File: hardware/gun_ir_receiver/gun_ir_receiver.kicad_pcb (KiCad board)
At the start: 2 copper layers, 19 x 17.8 mm, 3 parts

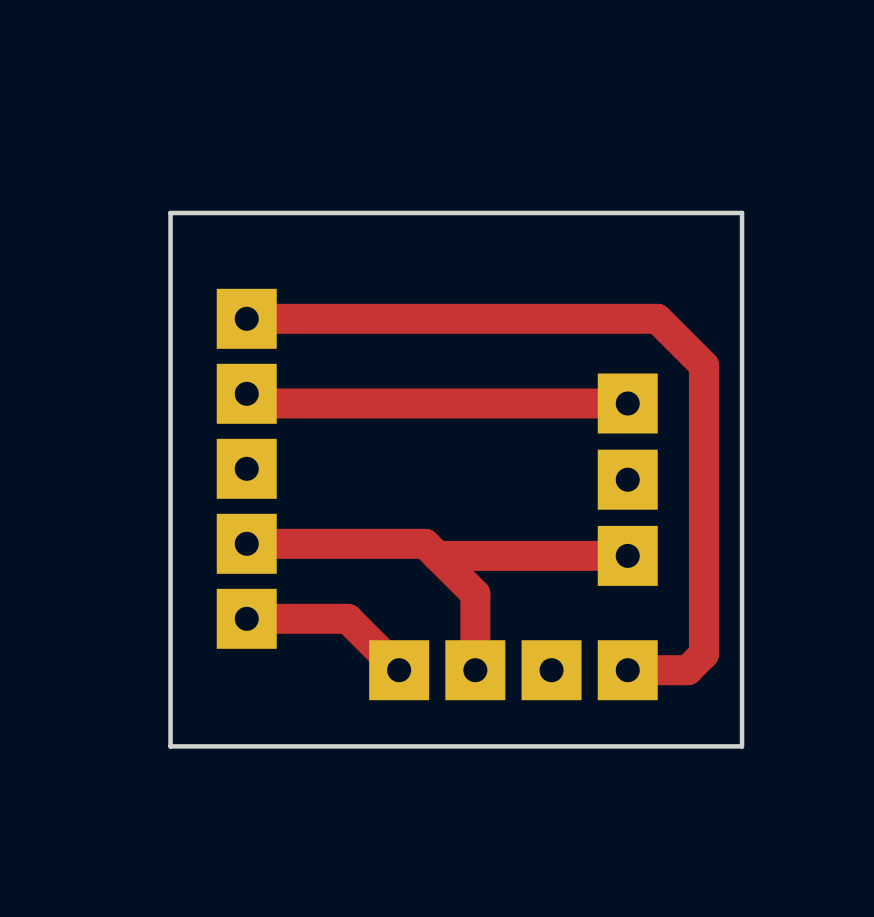
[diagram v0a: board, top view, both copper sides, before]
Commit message: Added led
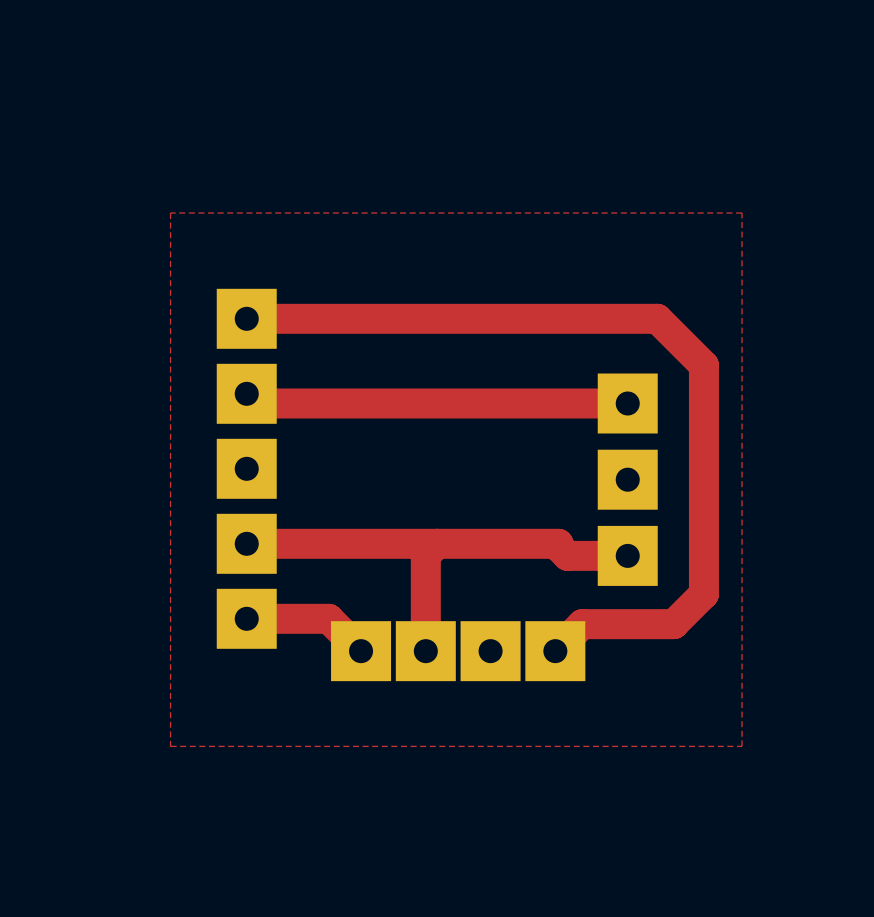
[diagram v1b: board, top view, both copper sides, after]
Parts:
- LEDPL9823: footprint Connector_PinSocket_2.54mm:PinSocket_1x04_P2.54mm_Vertical -> LED_THT:LED_D5.0mm-4_RGB_Wide_Pins
- moved LEDPL9823 1.42 mm to (118.1, 111.1), turned to 0 degrees
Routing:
- net /LedIn: track 5.79 -> 4.26 mm
- net /LedOut: track 28.3 -> 29.2 mm
- net +5V: track 17.2 -> 16.7 mm
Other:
- board outline removed
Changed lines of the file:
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@@
   (general
     (thickness 1.6)
-    (drawings 1)
-    (tracks 14)
+    (drawings 0)
+    (tracks 17)
     (zones 0)
     (modules 3)
@@
     (42 Eco1.User user)
     (43 Eco2.User user)
-    (44 Edge.Cuts user hide)
+    (44 Edge.Cuts user)
     (45 Margin user)
     (46 B.CrtYd user)
@@
     (add_net GND)
   )
-  (module Connector_PinSocket_2.54mm:PinSocket_1x04_P2.54mm_Vertical (layer B.Cu)
-    (at 119.38 111.76 270)
-    (descr "Through hole straight socket strip, 1x04, 2.54mm pitch, single row (from Kicad 4.0.7), script generated")
-    (tags "Through hole socket strip THT 1x04 2.54mm single row")
-    (fp_text reference LEDPL9823 (at 0 2.77 270) (layer B.SilkS)
-      (effects (font (size 1 1) (thickness 0.15)) (justify mirror))
-    )
-    (fp_text value Conn_01x04_Female (at 0 -10.39 270) (layer B.Fab)
-      (effects (font (size 1 1) (thickness 0.15)) (justify mirror))
-    )
-    (fp_line (start -1.27 1.27) (end 0.635 1.27) (layer B.Fab) (width 0.1))
-    (fp_line (start 0.635 1.27) (end 1.27 0.635) (layer B.Fab) (width 0.1))
-    (fp_line (start 1.27 0.635) (end 1.27 -8.89) (layer B.Fab) (width 0.1))
-    (fp_line (start 1.27 -8.89) (end -1.27 -8.89) (layer B.Fab) (width 0.1))
-    (fp_line (start -1.27 -8.89) (end -1.27 1.27) (layer B.Fab) (width 0.1))
-    (fp_line (start -1.33 -1.27) (end 1.33 -1.27) (layer B.SilkS) (width 0.12))
-    (fp_line (start -1.33 -1.27) (end -1.33 -8.95) (layer B.SilkS) (width 0.12))
-    (fp_line (start -1.33 -8.95) (end 1.33 -8.95) (layer B.SilkS) (width 0.12))
-    (fp_line (start 1.33 -1.27) (end 1.33 -8.95) (layer B.SilkS) (width 0.12))
-    (fp_line (start 1.33 1.33) (end 1.33 0) (layer B.SilkS) (width 0.12))
-    (fp_line (start 0 1.33) (end 1.33 1.33) (layer B.SilkS) (width 0.12))
-    (fp_line (start -1.8 1.8) (end 1.75 1.8) (layer B.CrtYd) (width 0.05))
-    (fp_line (start 1.75 1.8) (end 1.75 -9.4) (layer B.CrtYd) (width 0.05))
-    (fp_line (start 1.75 -9.4) (end -1.8 -9.4) (layer B.CrtYd) (width 0.05))
-    (fp_line (start -1.8 -9.4) (end -1.8 1.8) (layer B.CrtYd) (width 0.05))
-    (fp_text user %R (at 0 -3.81 180) (layer B.Fab)
-      (effects (font (size 1 1) (thickness 0.15)) (justify mirror))
-    )
-    (pad 1 thru_hole rect (at 0 0 270) (size 2 2) (drill 0.8) (layers *.Cu *.Mask)
+  (module LED_THT:LED_D5.0mm-4_RGB_Wide_Pins (layer B.Cu)
+    (at 118.11 111.125)
+    (descr "LED, diameter 5.0mm, 2 pins, diameter 5.0mm, 3 pins, diameter 5.0mm, 4 pins, http://www.kingbright.com/attachments/file/psearch/000/00/00/L-154A4SUREQBFZGEW(Ver.9A).pdf")
+    (tags "LED diameter 5.0mm 2 pins diameter 5.0mm 3 pins diameter 5.0mm 4 pins RGB RGBLED")
+    (fp_text reference LEDPL9823 (at 3.2385 3.96) (layer B.SilkS)
+      (effects (font (size 1 1) (thickness 0.15)) (justify mirror))
+    )
+    (fp_text value Conn_01x04_Female (at 3.2385 -3.96) (layer B.Fab)
+      (effects (font (size 1 1) (thickness 0.15)) (justify mirror))
+    )
+    (fp_arc (start 3.2385 0) (end 0.7385 1.469694) (angle -299.1) (layer B.Fab) (width 0.1))
+    (fp_arc (start 3.2385 0) (end 0.6785 1.54483) (angle -127.7) (layer B.SilkS) (width 0.12))
+    (fp_arc (start 3.2385 0) (end 0.6785 -1.54483) (angle 127.7) (layer B.SilkS) (width 0.12))
+    (fp_arc (start 3.2385 0) (end 0.983816 1.08) (angle -128.8) (layer B.SilkS) (width 0.12))
+    (fp_arc (start 3.2385 0) (end 0.983816 -1.08) (angle 128.8) (layer B.SilkS) (width 0.12))
+    (fp_circle (center 3.2385 0) (end 5.7385 0) (layer B.Fab) (width 0.1))
+    (fp_line (start 0.7385 1.469694) (end 0.7385 -1.469694) (layer B.Fab) (width 0.1))
+    (fp_line (start 0.6785 1.545) (end 0.6785 1.08) (layer B.SilkS) (width 0.12))
+    (fp_line (start 0.6785 -1.08) (end 0.6785 -1.545) (layer B.SilkS) (width 0.12))
+    (fp_line (start -1.08 3.25) (end -1.08 -3.25) (layer B.CrtYd) (width 0.05))
+    (fp_line (start -1.08 -3.25) (end 7.56 -3.25) (layer B.CrtYd) (width 0.05))
+    (fp_line (start 7.56 -3.25) (end 7.56 3.25) (layer B.CrtYd) (width 0.05))
+    (fp_line (start 7.56 3.25) (end -1.08 3.25) (layer B.CrtYd) (width 0.05))
+    (fp_text user %R (at 3.2385 3.96) (layer B.Fab)
+      (effects (font (size 1 1) (thickness 0.15)) (justify mirror))
+    )
+    (pad 1 thru_hole rect (at 0 0) (size 2 2) (drill 0.8) (layers *.Cu *.Mask)
       (net 5 /LedIn))
-    (pad 2 thru_hole rect (at 0 -2.54 270) (size 2 2) (drill 0.8) (layers *.Cu *.Mask)
+    (pad 2 thru_hole rect (at 2.159 0) (size 2 2) (drill 0.8) (layers *.Cu *.Mask)
       (net 2 +5V))
-    (pad 3 thru_hole rect (at 0 -5.08 270) (size 2 2) (drill 0.8) (layers *.Cu *.Mask)
+    (pad 3 thru_hole rect (at 4.318 0) (size 2 2) (drill 0.8) (layers *.Cu *.Mask)
       (net 4 GND))
-    (pad 4 thru_hole rect (at 0 -7.62 270) (size 2 2) (drill 0.8) (layers *.Cu *.Mask)
+    (pad 4 thru_hole rect (at 6.477 0) (size 2 2) (drill 0.8) (layers *.Cu *.Mask)
       (net 3 /LedOut))
-    (model ${KISYS3DMOD}/Connector_PinSocket_2.54mm.3dshapes/PinSocket_1x04_P2.54mm_Vertical.wrl
+    (model ${KISYS3DMOD}/LED_THT.3dshapes/LED_D5.0mm-4_RGB_Wide_Pins.wrl
       (at (xyz 0 0 0))
       (scale (xyz 1 1 1))
@@
     )
   )
-  (gr_poly (pts (xy 111.76 96.52) (xy 130.81 96.52) (xy 130.81 114.3) (xy 111.76 114.3)) (layer Edge.Cuts) (width 0.15))
   (segment (start 114.622704 102.87) (end 114.3 102.547296) (width 1) (layer F.Cu) (net 1))
   (segment (start 127 102.87) (end 114.622704 102.87) (width 1) (layer F.Cu) (net 1))
-  (segment (start 114.3 107.547296) (end 120.247296 107.547296) (width 1) (layer F.Cu) (net 2))
-  (segment (start 121.92 109.22) (end 121.92 111.76) (width 1) (layer F.Cu) (net 2))
-  (segment (start 120.65 107.95) (end 127 107.95) (width 1) (layer F.Cu) (net 2))
-  (segment (start 120.65 107.95) (end 121.92 109.22) (width 1) (layer F.Cu) (net 2))
-  (segment (start 120.247296 107.547296) (end 120.65 107.95) (width 1) (layer F.Cu) (net 2))
+  (segment (start 125 107.95) (end 127 107.95) (width 1) (layer F.Cu) (net 2))
+  (segment (start 124.692296 107.642296) (end 125 107.95) (width 1) (layer F.Cu) (net 2))
+  (segment (start 124.692296 107.547296) (end 124.692296 107.642296) (width 1) (layer F.Cu) (net 2))
+  (segment (start 120.269 107.928296) (end 120.65 107.547296) (width 1) (layer F.Cu) (net 2))
+  (segment (start 120.269 111.125) (end 120.269 107.928296) (width 1) (layer F.Cu) (net 2))
+  (segment (start 114.3 107.547296) (end 120.65 107.547296) (width 1) (layer F.Cu) (net 2))
+  (segment (start 120.65 107.547296) (end 124.692296 107.547296) (width 1) (layer F.Cu) (net 2))
+  (segment (start 125.486999 110.225001) (end 128.534999 110.225001) (width 1) (layer F.Cu) (net 3))
+  (segment (start 124.587 111.125) (end 125.486999 110.225001) (width 1) (layer F.Cu) (net 3))
+  (segment (start 128.534999 110.225001) (end 129.54 109.22) (width 1) (layer F.Cu) (net 3))
+  (segment (start 129.54 109.22) (end 129.54 101.6) (width 1) (layer F.Cu) (net 3))
   (segment (start 127.987296 100.047296) (end 114.3 100.047296) (width 1) (layer F.Cu) (net 3))
   (segment (start 129.54 101.6) (end 127.987296 100.047296) (width 1) (layer F.Cu) (net 3))
-  (segment (start 129.54 111.22) (end 129.54 101.6) (width 1) (layer F.Cu) (net 3))
-  (segment (start 127 111.76) (end 129 111.76) (width 1) (layer F.Cu) (net 3))
-  (segment (start 129 111.76) (end 129.54 111.22) (width 1) (layer F.Cu) (net 3))
-  (segment (start 117.667296 110.047296) (end 119.38 111.76) (width 1) (layer F.Cu) (net 5))
-  (segment (start 114.3 110.047296) (end 117.667296 110.047296) (width 1) (layer F.Cu) (net 5))
+  (segment (start 117.032296 110.047296) (end 118.11 111.125) (width 1) (layer F.Cu) (net 5))
+  (segment (start 114.3 110.047296) (end 117.032296 110.047296) (width 1) (layer F.Cu) (net 5))
   (zone (net 4) (net_name GND) (layer F.Cu) (hatch edge 0.508)
     (connect_pads yes (clearance 0.544))
@@
     (polygon
       (pts
-        (xy 111.76 96.52) (xy 130.81 96.506127) (xy 130.81 114.286127) (xy 111.76 114.3)
+        (xy 111.76 114.3) (xy 130.81 114.3) (xy 130.81 96.52) (xy 111.76 96.52)
       )
     )

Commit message: Added led
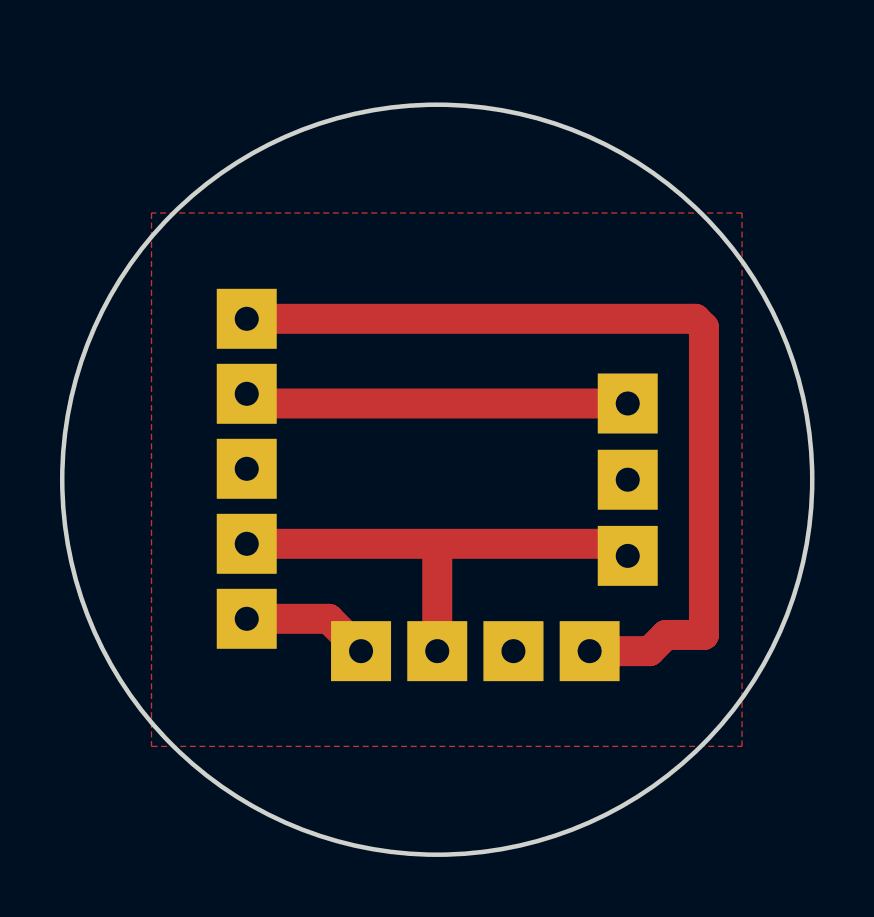
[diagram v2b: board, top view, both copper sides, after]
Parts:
- LEDPL9823: footprint LED_THT:LED_D5.0mm-4_RGB_Wide_Pins -> Connector_PinSocket_2.54mm:PinSocket_1x04_P2.54mm_Vertical
- turned LEDPL9823 to 270 degrees
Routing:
- net +5V: track 16.7 -> 16.0 mm
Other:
- board outline added: 25 x 25 mm
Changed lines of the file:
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@@
   (general
     (thickness 1.6)
-    (drawings 0)
-    (tracks 17)
+    (drawings 2)
+    (tracks 13)
     (zones 0)
     (modules 3)
@@
     (pad_to_mask_clearance 0.051)
     (solder_mask_min_width 0.25)
-    (aux_axis_origin 111.76 114.3)
+    (aux_axis_origin 111.125 114.3)
     (visible_elements FFFFFF7F)
     (pcbplotparams
@@
     (add_net GND)
   )
-  (module LED_THT:LED_D5.0mm-4_RGB_Wide_Pins (layer B.Cu)
-    (at 118.11 111.125)
-    (descr "LED, diameter 5.0mm, 2 pins, diameter 5.0mm, 3 pins, diameter 5.0mm, 4 pins, http://www.kingbright.com/attachments/file/psearch/000/00/00/L-154A4SUREQBFZGEW(Ver.9A).pdf")
-    (tags "LED diameter 5.0mm 2 pins diameter 5.0mm 3 pins diameter 5.0mm 4 pins RGB RGBLED")
-    (fp_text reference LEDPL9823 (at 3.2385 3.96) (layer B.SilkS)
-      (effects (font (size 1 1) (thickness 0.15)) (justify mirror))
-    )
-    (fp_text value Conn_01x04_Female (at 3.2385 -3.96) (layer B.Fab)
-      (effects (font (size 1 1) (thickness 0.15)) (justify mirror))
-    )
-    (fp_arc (start 3.2385 0) (end 0.7385 1.469694) (angle -299.1) (layer B.Fab) (width 0.1))
-    (fp_arc (start 3.2385 0) (end 0.6785 1.54483) (angle -127.7) (layer B.SilkS) (width 0.12))
-    (fp_arc (start 3.2385 0) (end 0.6785 -1.54483) (angle 127.7) (layer B.SilkS) (width 0.12))
-    (fp_arc (start 3.2385 0) (end 0.983816 1.08) (angle -128.8) (layer B.SilkS) (width 0.12))
-    (fp_arc (start 3.2385 0) (end 0.983816 -1.08) (angle 128.8) (layer B.SilkS) (width 0.12))
-    (fp_circle (center 3.2385 0) (end 5.7385 0) (layer B.Fab) (width 0.1))
-    (fp_line (start 0.7385 1.469694) (end 0.7385 -1.469694) (layer B.Fab) (width 0.1))
-    (fp_line (start 0.6785 1.545) (end 0.6785 1.08) (layer B.SilkS) (width 0.12))
-    (fp_line (start 0.6785 -1.08) (end 0.6785 -1.545) (layer B.SilkS) (width 0.12))
-    (fp_line (start -1.08 3.25) (end -1.08 -3.25) (layer B.CrtYd) (width 0.05))
-    (fp_line (start -1.08 -3.25) (end 7.56 -3.25) (layer B.CrtYd) (width 0.05))
-    (fp_line (start 7.56 -3.25) (end 7.56 3.25) (layer B.CrtYd) (width 0.05))
-    (fp_line (start 7.56 3.25) (end -1.08 3.25) (layer B.CrtYd) (width 0.05))
-    (fp_text user %R (at 3.2385 3.96) (layer B.Fab)
-      (effects (font (size 1 1) (thickness 0.15)) (justify mirror))
-    )
-    (pad 1 thru_hole rect (at 0 0) (size 2 2) (drill 0.8) (layers *.Cu *.Mask)
+  (module Connector_PinSocket_2.54mm:PinSocket_1x04_P2.54mm_Vertical (layer B.Cu)
+    (at 118.11 111.125 270)
+    (descr "Through hole straight socket strip, 1x04, 2.54mm pitch, single row (from Kicad 4.0.7), script generated")
+    (tags "Through hole socket strip THT 1x04 2.54mm single row")
+    (fp_text reference LEDPL9823 (at 0 2.77 270) (layer B.SilkS)
+      (effects (font (size 1 1) (thickness 0.15)) (justify mirror))
+    )
+    (fp_text value Conn_01x04_Female (at 0 -10.39 270) (layer B.Fab)
+      (effects (font (size 1 1) (thickness 0.15)) (justify mirror))
+    )
+    (fp_line (start -1.27 1.27) (end 0.635 1.27) (layer B.Fab) (width 0.1))
+    (fp_line (start 0.635 1.27) (end 1.27 0.635) (layer B.Fab) (width 0.1))
+    (fp_line (start 1.27 0.635) (end 1.27 -8.89) (layer B.Fab) (width 0.1))
+    (fp_line (start 1.27 -8.89) (end -1.27 -8.89) (layer B.Fab) (width 0.1))
+    (fp_line (start -1.27 -8.89) (end -1.27 1.27) (layer B.Fab) (width 0.1))
+    (fp_line (start -1.33 -1.27) (end 1.33 -1.27) (layer B.SilkS) (width 0.12))
+    (fp_line (start -1.33 -1.27) (end -1.33 -8.95) (layer B.SilkS) (width 0.12))
+    (fp_line (start -1.33 -8.95) (end 1.33 -8.95) (layer B.SilkS) (width 0.12))
+    (fp_line (start 1.33 -1.27) (end 1.33 -8.95) (layer B.SilkS) (width 0.12))
+    (fp_line (start 1.33 1.33) (end 1.33 0) (layer B.SilkS) (width 0.12))
+    (fp_line (start 0 1.33) (end 1.33 1.33) (layer B.SilkS) (width 0.12))
+    (fp_line (start -1.8 1.8) (end 1.75 1.8) (layer B.CrtYd) (width 0.05))
+    (fp_line (start 1.75 1.8) (end 1.75 -9.4) (layer B.CrtYd) (width 0.05))
+    (fp_line (start 1.75 -9.4) (end -1.8 -9.4) (layer B.CrtYd) (width 0.05))
+    (fp_line (start -1.8 -9.4) (end -1.8 1.8) (layer B.CrtYd) (width 0.05))
+    (fp_text user %R (at 0 -3.81 180) (layer B.Fab)
+      (effects (font (size 1 1) (thickness 0.15)) (justify mirror))
+    )
+    (pad 1 thru_hole rect (at 0 0 270) (size 2 2) (drill 0.8) (layers *.Cu *.Mask)
       (net 5 /LedIn))
-    (pad 2 thru_hole rect (at 2.159 0) (size 2 2) (drill 0.8) (layers *.Cu *.Mask)
+    (pad 2 thru_hole rect (at 0 -2.54 270) (size 2 2) (drill 0.8) (layers *.Cu *.Mask)
       (net 2 +5V))
-    (pad 3 thru_hole rect (at 4.318 0) (size 2 2) (drill 0.8) (layers *.Cu *.Mask)
+    (pad 3 thru_hole rect (at 0 -5.08 270) (size 2 2) (drill 0.8) (layers *.Cu *.Mask)
       (net 4 GND))
-    (pad 4 thru_hole rect (at 6.477 0) (size 2 2) (drill 0.8) (layers *.Cu *.Mask)
+    (pad 4 thru_hole rect (at 0 -7.62 270) (size 2 2) (drill 0.8) (layers *.Cu *.Mask)
       (net 3 /LedOut))
-    (model ${KISYS3DMOD}/LED_THT.3dshapes/LED_D5.0mm-4_RGB_Wide_Pins.wrl
+    (model ${KISYS3DMOD}/Connector_PinSocket_2.54mm.3dshapes/PinSocket_1x04_P2.54mm_Vertical.wrl
       (at (xyz 0 0 0))
       (scale (xyz 1 1 1))
@@
     )
   )
+  (dimension 19.812 (width 0.3) (layer Dwgs.User)
+    (gr_text "19,812 mm" (at 120.904 91.372) (layer Dwgs.User)
+      (effects (font (size 1.5 1.5) (thickness 0.3)))
+    )
+    (feature1 (pts (xy 130.81 95.504) (xy 130.81 92.885579)))
+    (feature2 (pts (xy 110.998 95.504) (xy 110.998 92.885579)))
+    (crossbar (pts (xy 110.998 93.472) (xy 130.81 93.472)))
+    (arrow1a (pts (xy 130.81 93.472) (xy 129.683496 94.058421)))
+    (arrow1b (pts (xy 130.81 93.472) (xy 129.683496 92.885579)))
+    (arrow2a (pts (xy 110.998 93.472) (xy 112.124504 94.058421)))
+    (arrow2b (pts (xy 110.998 93.472) (xy 112.124504 92.885579)))
+  )
+  (gr_circle (center 120.65 105.41) (end 133.15 105.41) (layer Edge.Cuts) (width 0.15))
   (segment (start 114.622704 102.87) (end 114.3 102.547296) (width 1) (layer F.Cu) (net 1))
   (segment (start 127 102.87) (end 114.622704 102.87) (width 1) (layer F.Cu) (net 1))
-  (segment (start 125 107.95) (end 127 107.95) (width 1) (layer F.Cu) (net 2))
-  (segment (start 124.692296 107.642296) (end 125 107.95) (width 1) (layer F.Cu) (net 2))
-  (segment (start 124.692296 107.547296) (end 124.692296 107.642296) (width 1) (layer F.Cu) (net 2))
-  (segment (start 120.269 107.928296) (end 120.65 107.547296) (width 1) (layer F.Cu) (net 2))
-  (segment (start 120.269 111.125) (end 120.269 107.928296) (width 1) (layer F.Cu) (net 2))
-  (segment (start 114.3 107.547296) (end 120.65 107.547296) (width 1) (layer F.Cu) (net 2))
-  (segment (start 120.65 107.547296) (end 124.692296 107.547296) (width 1) (layer F.Cu) (net 2))
-  (segment (start 125.486999 110.225001) (end 128.534999 110.225001) (width 1) (layer F.Cu) (net 3))
-  (segment (start 124.587 111.125) (end 125.486999 110.225001) (width 1) (layer F.Cu) (net 3))
-  (segment (start 128.534999 110.225001) (end 129.54 109.22) (width 1) (layer F.Cu) (net 3))
-  (segment (start 129.54 109.22) (end 129.54 101.6) (width 1) (layer F.Cu) (net 3))
-  (segment (start 127.987296 100.047296) (end 114.3 100.047296) (width 1) (layer F.Cu) (net 3))
-  (segment (start 129.54 101.6) (end 127.987296 100.047296) (width 1) (layer F.Cu) (net 3))
+  (segment (start 126.597296 107.547296) (end 127 107.95) (width 1) (layer F.Cu) (net 2))
+  (segment (start 114.3 107.547296) (end 126.597296 107.547296) (width 1) (layer F.Cu) (net 2))
+  (segment (start 120.65 111.125) (end 120.65 107.95) (width 1) (layer F.Cu) (net 2))
+  (segment (start 129.54 110.585) (end 129.54 100.33) (width 1) (layer F.Cu) (net 3))
+  (segment (start 129.257296 100.047296) (end 114.3 100.047296) (width 1) (layer F.Cu) (net 3))
+  (segment (start 129.54 100.33) (end 129.257296 100.047296) (width 1) (layer F.Cu) (net 3))
+  (segment (start 128.27 110.585) (end 129.54 110.585) (width 1) (layer F.Cu) (net 3))
+  (segment (start 127.73 111.125) (end 128.27 110.585) (width 1) (layer F.Cu) (net 3))
+  (segment (start 125.73 111.125) (end 127.73 111.125) (width 1) (layer F.Cu) (net 3))
   (segment (start 117.032296 110.047296) (end 118.11 111.125) (width 1) (layer F.Cu) (net 5))
   (segment (start 114.3 110.047296) (end 117.032296 110.047296) (width 1) (layer F.Cu) (net 5))
@@
     (polygon
       (pts
-        (xy 111.76 114.3) (xy 130.81 114.3) (xy 130.81 96.52) (xy 111.76 96.52)
+        (xy 111.125 114.3) (xy 130.81 114.3) (xy 130.81 96.52) (xy 111.125 96.52)
       )
     )
